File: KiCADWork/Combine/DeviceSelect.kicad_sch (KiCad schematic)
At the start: 30 parts, among them U1 USB2422T-I/MJ, U5 SIP32509DT-T1-GE3, U6 SIP32509DT-T1-GE3, Y1 X322524MOB4SI

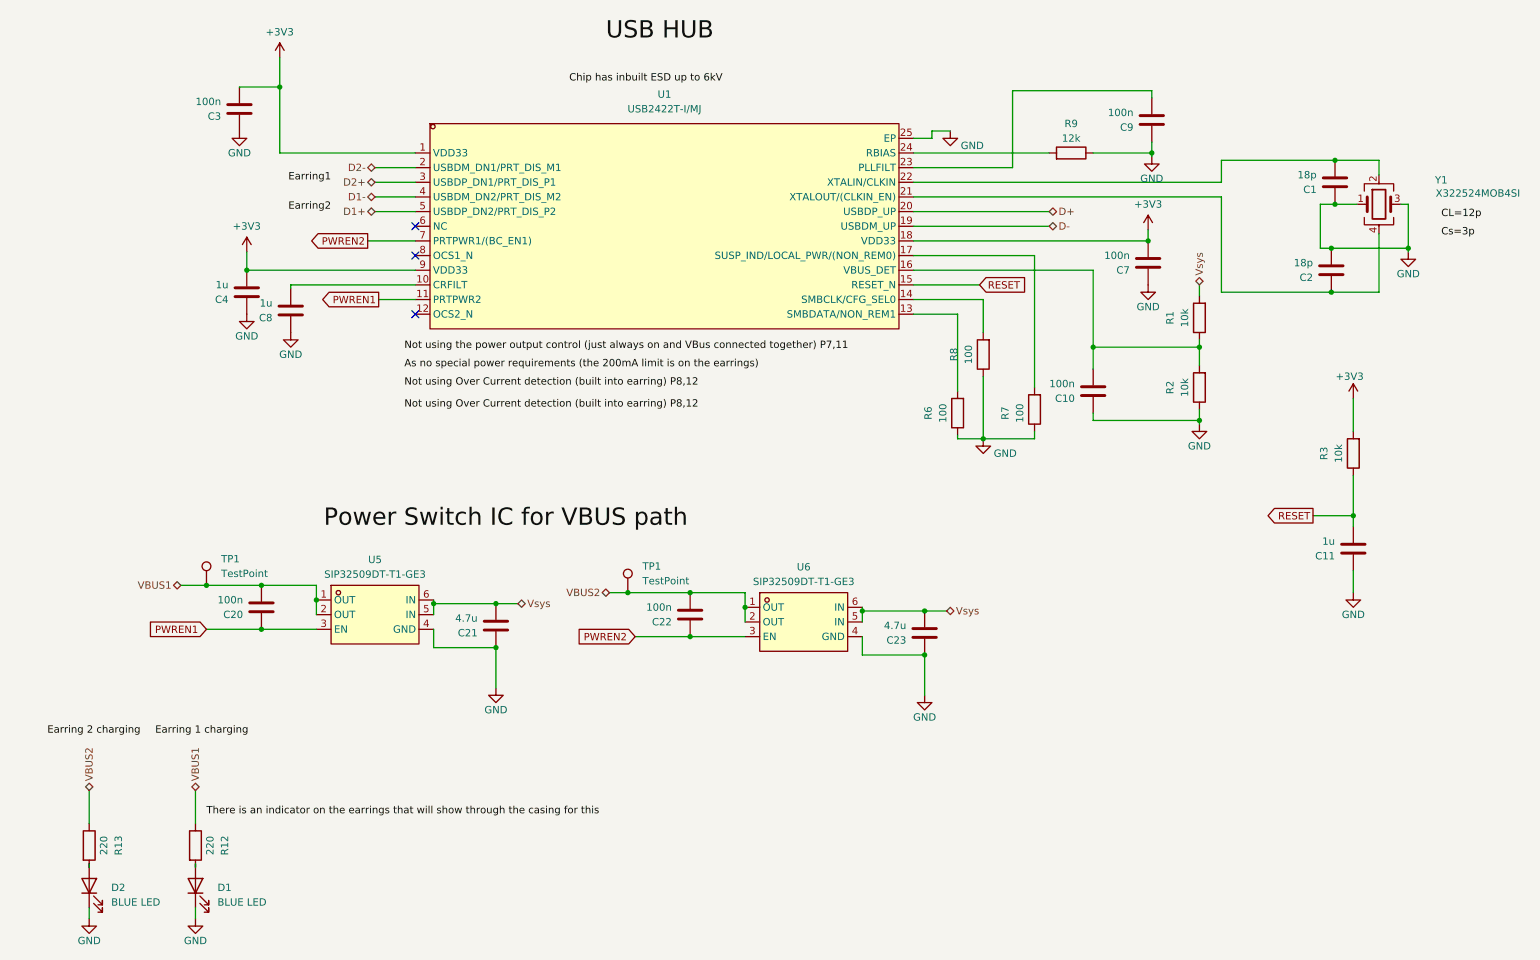
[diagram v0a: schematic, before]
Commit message: Completing the combined layout
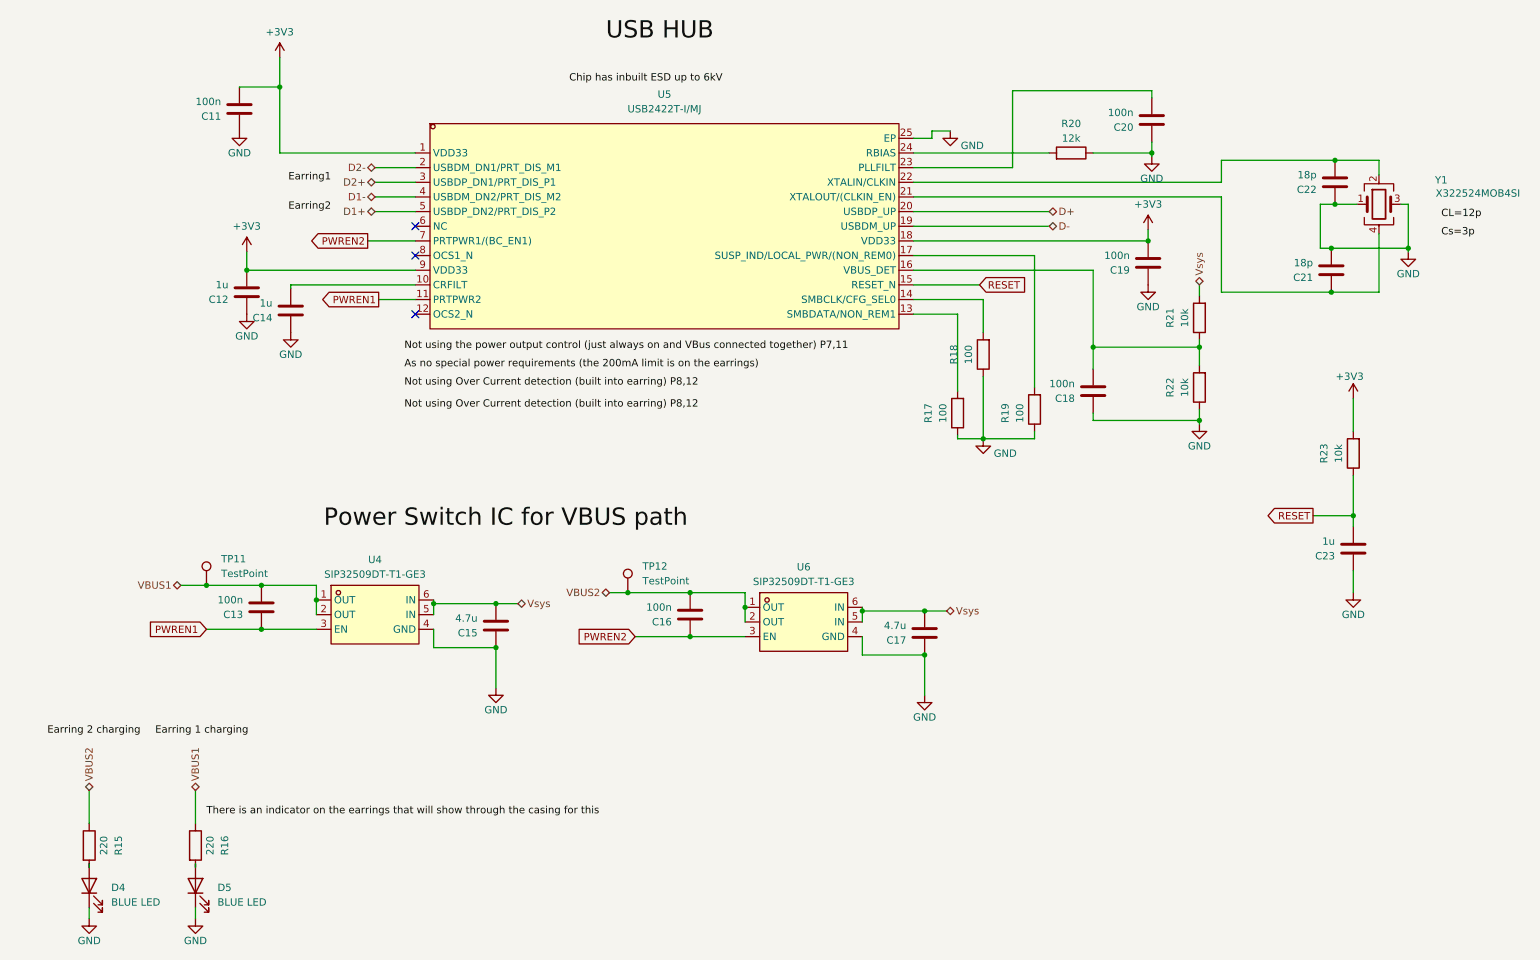
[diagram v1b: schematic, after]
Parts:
- renumbered C3 to C11, C4 to C12, C20 to C13, C8 to C14, C21 to C15, C22 to C16, C23 to C17, C10 to C18, C7 to C19, C9 to C20, C2 to C21, C1 to C22, C11 to C23, D2 to D4, D1 to D5, R13 to R15, R12 to R16, R6 to R17, R8 to R18, R7 to R19, R9 to R20, R1 to R21, R2 to R22, R3 to R23, TP1 to TP11, TP1 to TP12, U5 to U4, U1 to U5

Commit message: Schem rev 1 pt1
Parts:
- added TP27, TP28: TestPoint, TestPoint:TestPoint_Pad_D1.0mm, symbol Connector:TestPoint
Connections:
- net D1+: now also U5.3 (USBDP_DN1/PRT_DIS_P1); no longer U5.5 (USBDP_DN2/PRT_DIS_P2)
- net D1-: now also U5.2 (USBDM_DN1/PRT_DIS_M1); no longer U5.4 (USBDM_DN2/PRT_DIS_M2)
- net D2+: now also U5.5 (USBDP_DN2/PRT_DIS_P2); no longer U5.3 (USBDP_DN1/PRT_DIS_P1)
- net D2-: now also U5.4 (USBDM_DN2/PRT_DIS_M2); no longer U5.2 (USBDM_DN1/PRT_DIS_M1)
- net GND: now also C13.1, C16.1
- net PWREN1: now also TP27.1; no longer C13.1
- net PWREN2: now also TP28.1; no longer C16.1
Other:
- moved on the sheet: C13, C16
